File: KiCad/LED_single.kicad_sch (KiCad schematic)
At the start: 8 parts, among them U112 2N7002, U113 2N7002

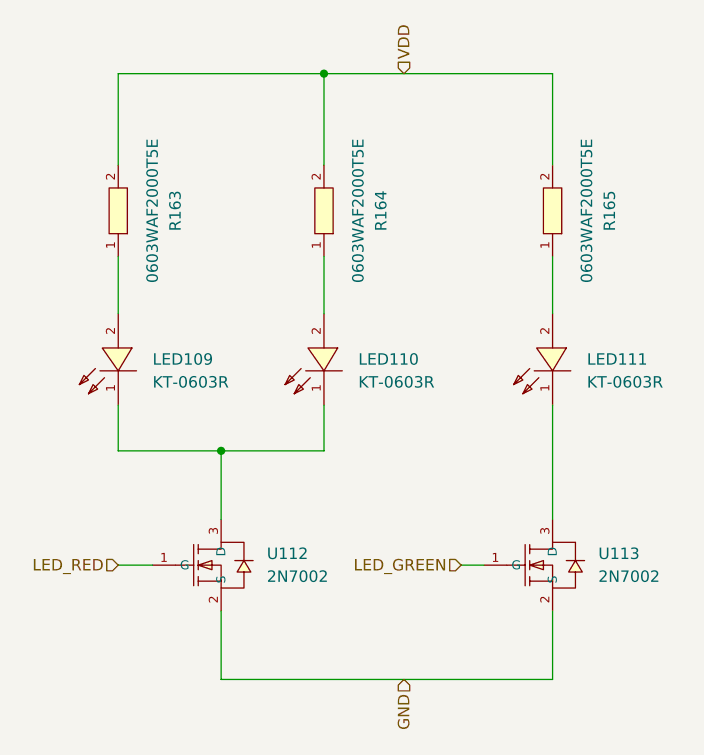
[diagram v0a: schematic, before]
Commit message: Ready for PCB layout with discreet LEDs
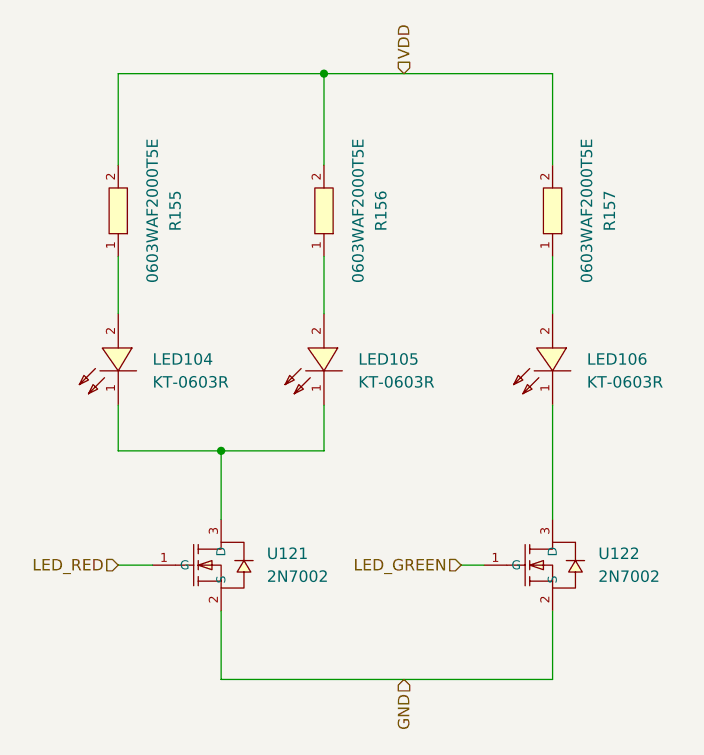
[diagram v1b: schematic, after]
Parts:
- renumbered LED109 to LED104, LED110 to LED105, LED111 to LED106, R163 to R155, R164 to R156, R165 to R157, U112 to U121, U113 to U122
